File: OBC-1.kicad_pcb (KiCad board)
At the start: 6 copper layers, 42.8 x 42.8 mm, 110 parts, among them J1 ERM8-020-X, J2 ERF6-020-X, J3 Conn_01x02_Female, Q1 MGSF1N02L, Q2 MGSF1N02L, U1 TPS62850x-Q1, U11 TMS5701227CZWTQQ1, U2 TPS62850x-Q1, U3 LTC4353, U4 SN65HVD230M-EP, U5 SN65HVD230M-EP, U6 SN65HVD230M-EP

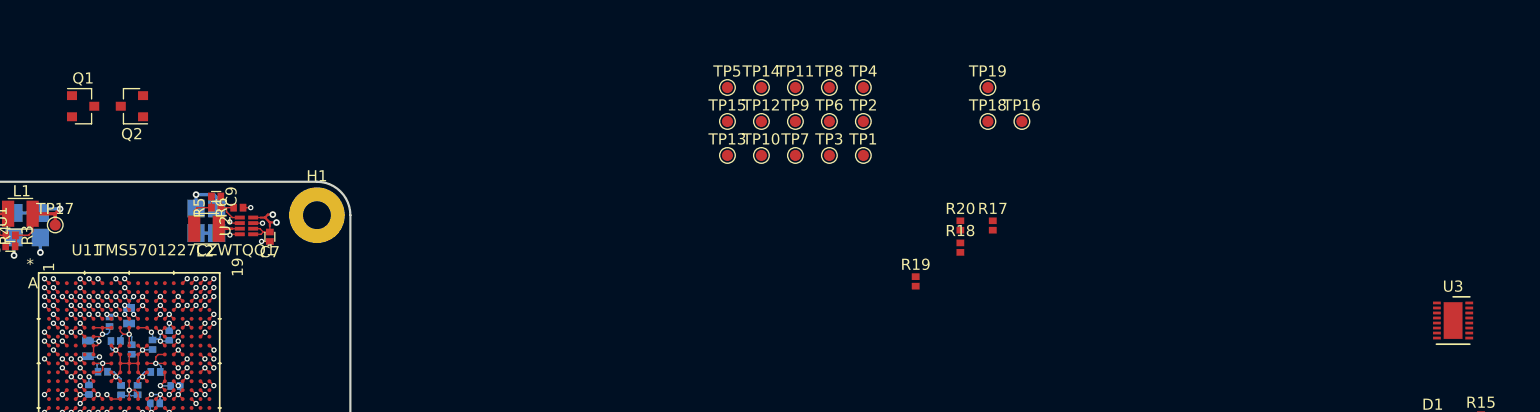
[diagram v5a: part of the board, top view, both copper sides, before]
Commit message: added testpoints to 2nd supply, positioned early floorplan for ORing diode controller, needs work - gates are on wrong sides - need to switch supply sides
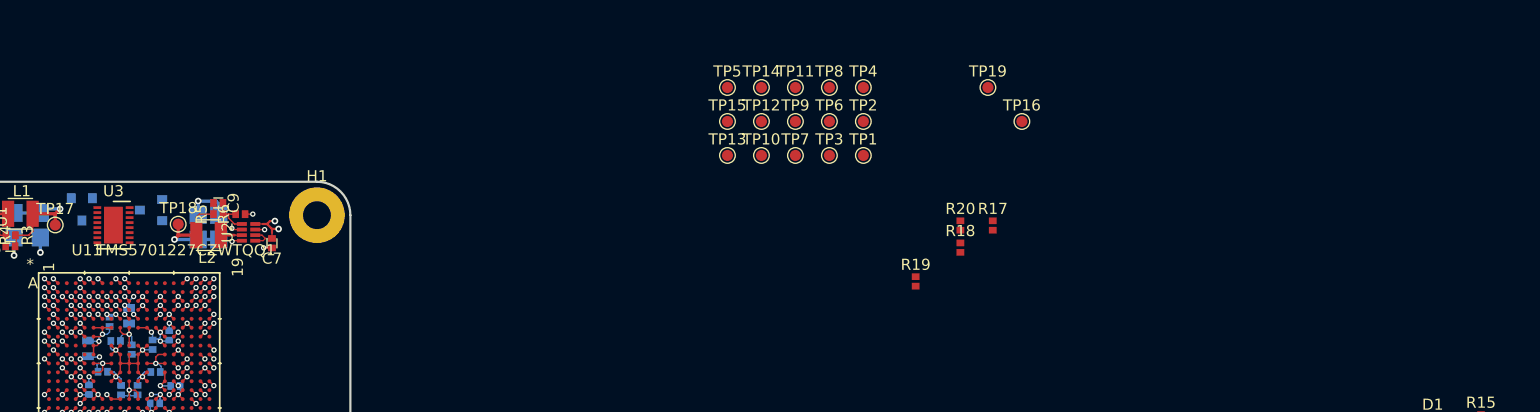
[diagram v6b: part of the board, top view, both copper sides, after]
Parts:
- Q1, Q2: moved to B.Cu
- moved U3 120.6 mm to (110.4, 75.4)
- moved TP18 73.3 mm to (116.2, 75.3)
- moved Q1 11.1 mm to (113.8, 74.0), turned to 180 degrees
- moved Q2 10.3 mm to (107.6, 74.0), turned to 270 degrees
- moved C11 0.61 mm to (119.9, 75.6)
- moved C13 0.61 mm to (118.0, 75.6)
- moved C7 0.61 mm to (124.7, 77.0)
- moved C9 0.61 mm to (119.8, 73.4)
- moved R5 0.61 mm to (119.8, 74.4)
- moved U2 0.61 mm to (123.2, 76.8)
- moved R6 0.61 mm to (121.8, 74.4)
- moved L2 0.61 mm to (119.0, 76.3)
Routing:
- net OBC_1V2_R: track 6.13 -> 11.4 mm, vias 0 -> 1

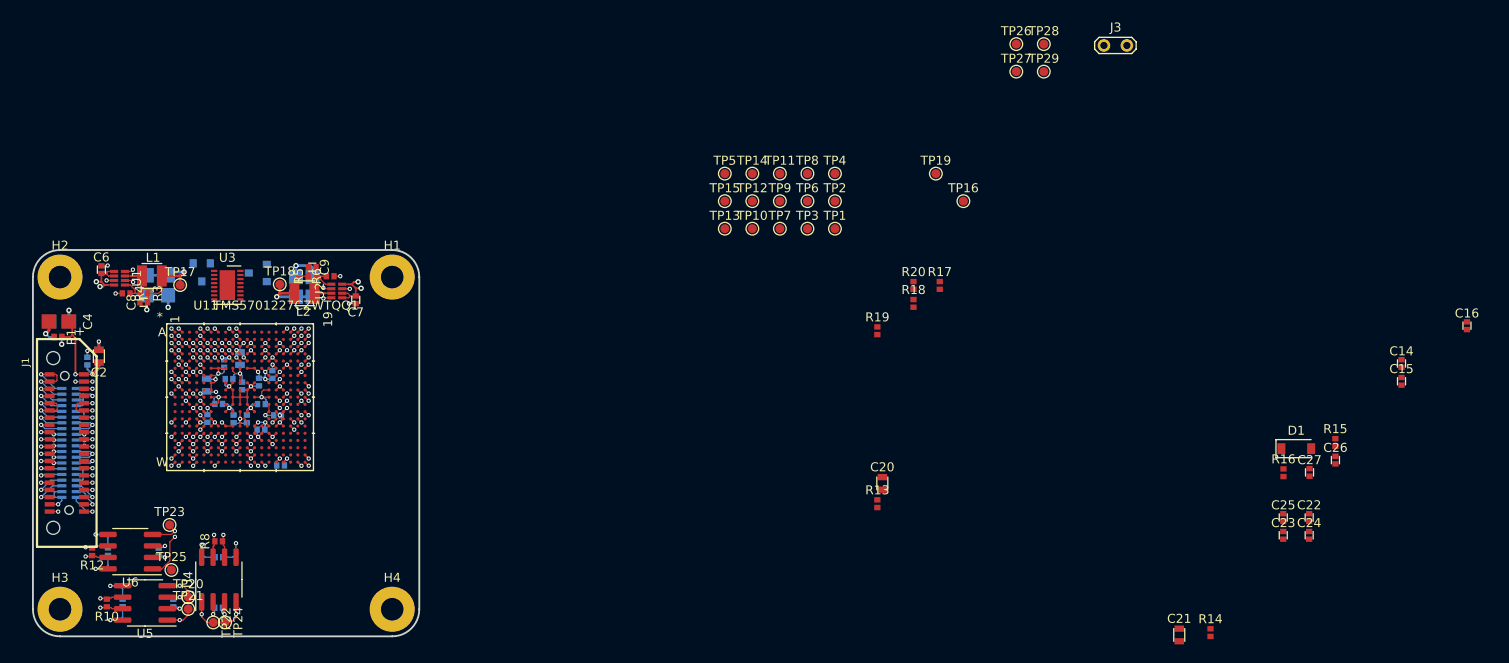
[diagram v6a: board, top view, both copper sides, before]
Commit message: updated CAN xcvr positions
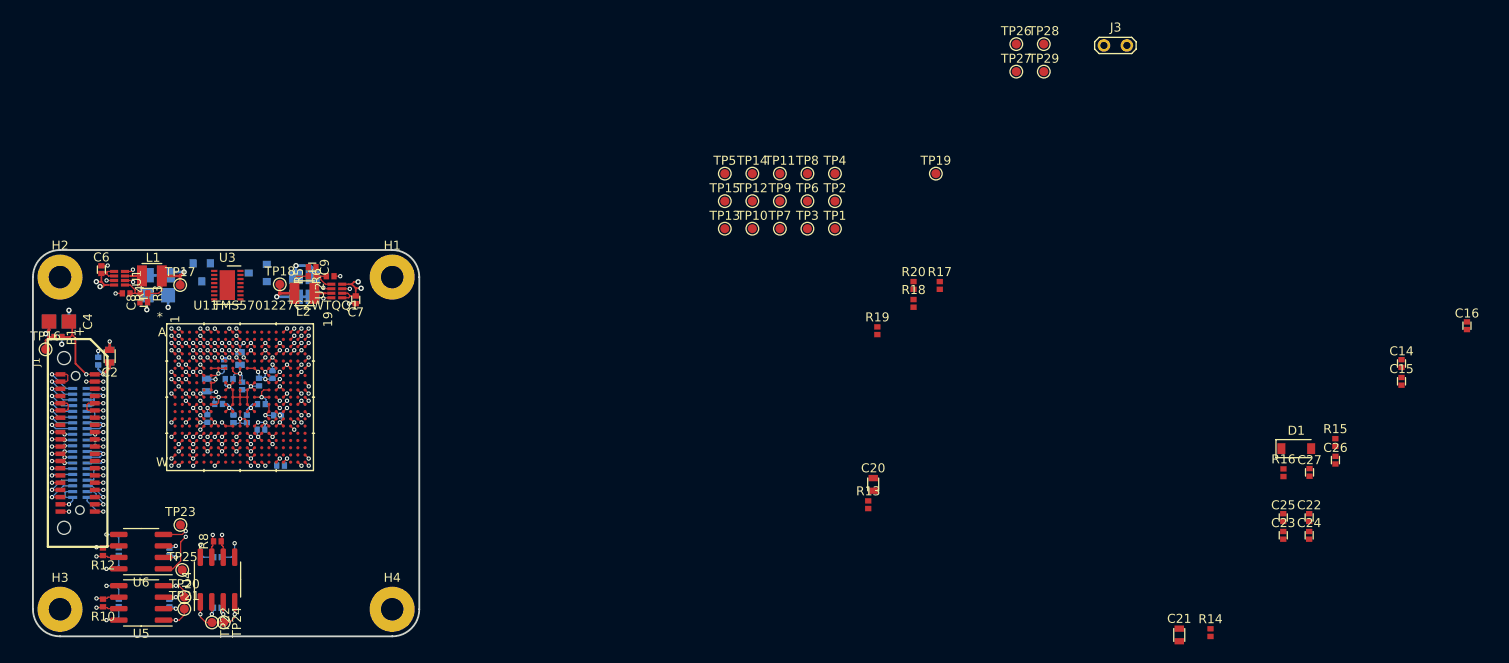
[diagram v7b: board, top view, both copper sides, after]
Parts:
- moved TP16 103.0 mm to (90.3, 82.5)
- moved C19 1.20 mm to (104.0, 104.9)
- moved C2 1.20 mm to (97.4, 83.3)
- moved C3 1.20 mm to (97.4, 83.3)
- moved R11 1.20 mm to (98.4, 104.9)
- moved R12 1.20 mm to (96.7, 104.9)
- moved TP23 1.20 mm to (105.2, 102.0)
- moved C1 1.20 mm to (96.1, 83.8)
- moved J1 1.20 mm to (93.8, 92.9)
- moved J2 1.20 mm to (94.1, 92.9)
- moved TP25 1.20 mm to (105.4, 106.9)
- moved U6 1.20 mm to (100.9, 104.9)
- moved C20 1.02 mm to (182.0, 97.5)
- moved R13 1.02 mm to (181.4, 99.7)
- moved C18 0.43 mm to (104.0, 110.6)
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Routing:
- net Net-(C4-Pad2): track 4.11 -> 6.71 mm
- net /CAN_XCVR_R/CAN_H_PL: track 19.8 -> 21.6 mm
- net /CAN_XCVR_R/CAN_L_PL: track 18.2 -> 19.9 mm
- net /CAN_XCVR_PL/CAN_L_PL: track 20.9 -> 19.5 mm
- net /CAN_XCVR_PL/CAN_H_PL: track 19.3 -> 18.4 mm

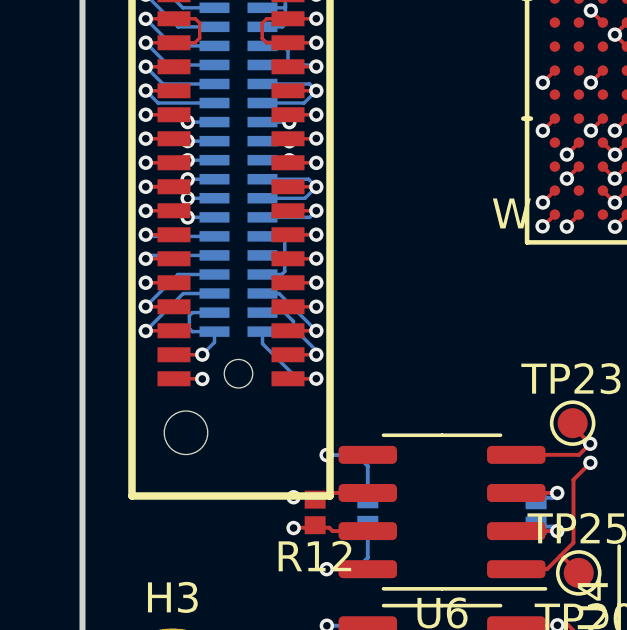
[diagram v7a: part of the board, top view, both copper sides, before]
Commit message: fixed wonky payload CAN bus routing
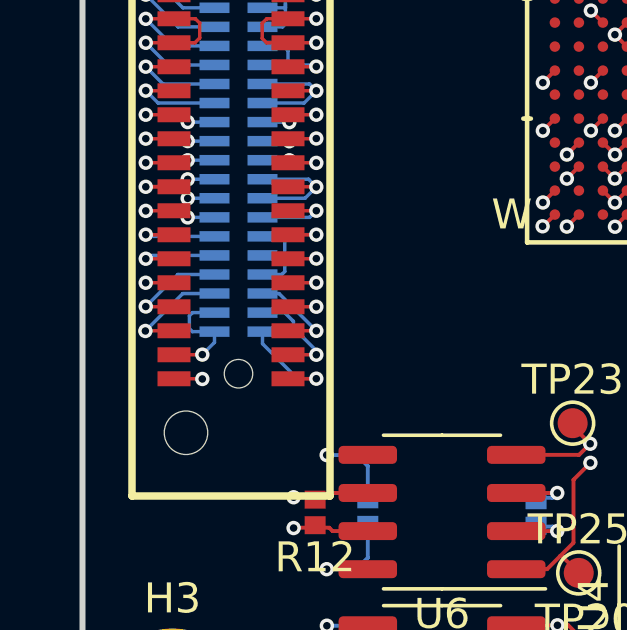
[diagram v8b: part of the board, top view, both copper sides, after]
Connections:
- J1 pad 23: /Connectors/CAN_H_PA -> /Connectors/CAN_L_PA
- J1 pad 24: /Connectors/CAN_L_PA -> /Connectors/CAN_H_PA
- J2 pad 23: /Connectors/CAN_H_PA -> /Connectors/CAN_L_PA
- J2 pad 24: /Connectors/CAN_L_PA -> /Connectors/CAN_H_PA
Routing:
- net /Connectors/CAN_L_PA: track 17.6 -> 15.9 mm
- net /Connectors/CAN_H_PA: track 16.9 -> 17.5 mm
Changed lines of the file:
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@@
     (thickness 1.6)
     (drawings 8)
-    (tracks 1281)
+    (tracks 1283)
     (zones 0)
     (modules 110)
@@
       (net 16 /CAN_XCVR_R/CAN_H_PL))
     (pad 23 smd rect (at 6 1.9 270) (size 0.5 1.1) (layers F.Cu F.Paste F.Mask)
-      (net 18 /Connectors/CAN_H_PA))
+      (net 19 /Connectors/CAN_L_PA))
     (pad 18 smd rect (at 6 -1.9 270) (size 0.5 1.1) (layers F.Cu F.Paste F.Mask)
       (net 2 GND))
     (pad 24 smd rect (at 5.2 1.9 270) (size 0.5 1.1) (layers F.Cu F.Paste F.Mask)
-      (net 19 /Connectors/CAN_L_PA))
+      (net 18 /Connectors/CAN_H_PA))
     (pad 17 smd rect (at 5.2 -1.9 270) (size 0.5 1.1) (layers F.Cu F.Paste F.Mask)
       (net 2 GND))
@@
       (net 2 GND))
     (pad 24 smd rect (at 4.1275 0.8 270) (size 0.35 1) (layers B.Cu B.Paste B.Mask)
-      (net 19 /Connectors/CAN_L_PA))
+      (net 18 /Connectors/CAN_H_PA))
     (pad 29 smd rect (at 0.9525 0.8 270) (size 0.35 1) (layers B.Cu B.Paste B.Mask)
       (net 2 GND))
     (pad 23 smd rect (at 4.7625 0.8 270) (size 0.35 1) (layers B.Cu B.Paste B.Mask)
-      (net 18 /Connectors/CAN_H_PA))
+      (net 19 /Connectors/CAN_L_PA))
     (pad 26 smd rect (at 2.8575 0.8 270) (size 0.35 1) (layers B.Cu B.Paste B.Mask)
       (net 2 GND))
@@
   (segment (start 96.6343 110.0963) (end 96.7534 110.0963) (width 0.13) (layer In3.Cu) (net 17))
   (segment (start 95.9406 110.0963) (end 96.6343 110.0963) (width 0.13) (layer In3.Cu) (net 17))
-  (via (at 91.00932 98.8822) (size 0.48) (drill 0.25) (layers F.Cu B.Cu) (net 18))
   (segment (start 96.6532 105.44048) (end 97.12564 105.44048) (width 0.13) (layer F.Cu) (net 18))
   (segment (start 97.2374 105.55224) (end 98.4088 105.55224) (width 0.13) (layer F.Cu) (net 18))
@@
   (segment (start 96.6532 105.44048) (end 95.94708 105.44048) (width 0.13) (layer F.Cu) (net 18))
   (via (at 95.93692 105.45064) (size 0.48) (drill 0.25) (layers F.Cu B.Cu) (net 18))
-  (segment (start 91.01652 98.875) (end 91.00932 98.8822) (width 0.115) (layer F.Cu) (net 18))
-  (segment (start 91.95 98.875) (end 91.01652 98.875) (width 0.115) (layer F.Cu) (net 18))
-  (segment (start 92.25702 97.6345) (end 91.00932 98.8822) (width 0.115) (layer B.Cu) (net 18))
-  (segment (start 93.3 97.6345) (end 92.25702 97.6345) (width 0.115) (layer B.Cu) (net 18))
-  (segment (start 92.45712 105.45064) (end 95.93692 105.45064) (width 0.13) (layer In2.Cu) (net 18))
-  (segment (start 91.01501 104.00853) (end 92.45712 105.45064) (width 0.13) (layer In2.Cu) (net 18))
-  (segment (start 91.01501 98.8822) (end 91.01501 104.00853) (width 0.13) (layer In2.Cu) (net 18))
-  (via (at 91.00932 98.06686) (size 0.48) (drill 0.25) (layers F.Cu B.Cu) (net 19))
+  (segment (start 91.0027 98.875) (end 90.995497 98.882203) (width 0.115) (layer F.Cu) (net 19))
+  (via (at 90.995497 98.882203) (size 0.48) (drill 0.25) (layers F.Cu B.Cu) (net 19))
+  (segment (start 91.95 98.875) (end 91.0027 98.875) (width 0.115) (layer F.Cu) (net 19))
+  (segment (start 93.3 97.6345) (end 92.2432 97.6345) (width 0.115) (layer B.Cu) (net 19))
+  (segment (start 92.2432 97.6345) (end 90.995497 98.882203) (width 0.115) (layer B.Cu) (net 19))
+  (via (at 91.00932 98.06686) (size 0.48) (drill 0.25) (layers F.Cu B.Cu) (net 18))
   (segment (start 96.6532 104.42048) (end 97.1144 104.42048) (width 0.13) (layer F.Cu) (net 19))
   (segment (start 97.25264 104.28224) (end 98.4088 104.28224) (width 0.13) (layer F.Cu) (net 19))
@@
   (via (at 95.93692 104.42448) (size 0.48) (drill 0.25) (layers F.Cu B.Cu) (net 19))
   (segment (start 96.6532 104.42048) (end 95.94092 104.42048) (width 0.13) (layer F.Cu) (net 19))
-  (segment (start 91.01746 98.075) (end 91.00932 98.06686) (width 0.115) (layer F.Cu) (net 19))
-  (segment (start 91.95 98.075) (end 91.01746 98.075) (width 0.115) (layer F.Cu) (net 19))
-  (segment (start 92.07668 96.9995) (end 91.00932 98.06686) (width 0.115) (layer B.Cu) (net 19))
-  (segment (start 93.3 96.9995) (end 92.07668 96.9995) (width 0.115) (layer B.Cu) (net 19))
-  (segment (start 91.464321 98.521861) (end 91.00932 98.06686) (width 0.13) (layer In3.Cu) (net 19))
-  (segment (start 91.464321 99.100601) (end 91.464321 98.521861) (width 0.13) (layer In3.Cu) (net 19))
-  (segment (start 91.01501 99.549912) (end 91.464321 99.100601) (width 0.13) (layer In3.Cu) (net 19))
-  (segment (start 91.01501 104.01361) (end 91.01501 99.549912) (width 0.13) (layer In3.Cu) (net 19))
-  (segment (start 91.42588 104.42448) (end 91.01501 104.01361) (width 0.13) (layer In3.Cu) (net 19))
-  (segment (start 95.93692 104.42448) (end 91.42588 104.42448) (width 0.13) (layer In3.Cu) (net 19))
+  (segment (start 91.01746 98.075) (end 91.00932 98.06686) (width 0.115) (layer F.Cu) (net 18))
+  (segment (start 91.95 98.075) (end 91.01746 98.075) (width 0.115) (layer F.Cu) (net 18))
+  (segment (start 92.07668 96.9995) (end 91.00932 98.06686) (width 0.115) (layer B.Cu) (net 18))
+  (segment (start 93.3 96.9995) (end 92.07668 96.9995) (width 0.115) (layer B.Cu) (net 18))
+  (segment (start 95.93692 105.45064) (end 95.53387 105.45064) (width 0.13) (layer In3.Cu) (net 18))
+  (segment (start 94.78772 104.70449) (end 92.827697 104.70449) (width 0.13) (layer In3.Cu) (net 18))
+  (segment (start 92.827697 104.70449) (end 92.56268 104.439472) (width 0.13) (layer In3.Cu) (net 18))
+  (segment (start 95.53387 105.45064) (end 94.78772 104.70449) (width 0.13) (layer In3.Cu) (net 18))
+  (segment (start 90.39799 98.67819) (end 91.00932 98.06686) (width 0.13) (layer In3.Cu) (net 18))
+  (segment (start 90.39799 102.274783) (end 90.39799 98.67819) (width 0.13) (layer In3.Cu) (net 18))
+  (segment (start 92.56268 104.439472) (end 90.39799 102.274783) (width 0.13) (layer In3.Cu) (net 18))
+  (segment (start 90.678 99.1997) (end 90.995497 98.882203) (width 0.13) (layer In3.Cu) (net 19))
+  (segment (start 90.678 102.1588) (end 90.678 99.1997) (width 0.13) (layer In3.Cu) (net 19))
+  (segment (start 92.94368 104.42448) (end 90.678 102.1588) (width 0.13) (layer In3.Cu) (net 19))
+  (segment (start 95.93692 104.42448) (end 92.94368 104.42448) (width 0.13) (layer In3.Cu) (net 19))
   (via (at 91.00932 94.87916) (size 0.48) (drill 0.25) (layers F.Cu B.Cu) (net 20))
   (segment (start 91.01348 94.875) (end 91.00932 94.87916) (width 0.115) (layer F.Cu) (net 20))
